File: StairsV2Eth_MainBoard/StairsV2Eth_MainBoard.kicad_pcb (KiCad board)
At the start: 2 copper layers, 102 x 86.2 mm, 104 parts, among them IC1 74HCT08D,653, IC2 74HCT08D,653, J10 Conn_01x02, J11 Conn_01x02, J12 Conn_01x02, J13 Conn_01x02, J14 Conn_01x18, J15 Conn_01x04, J16 Conn_01x04, J2 Conn_01x02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

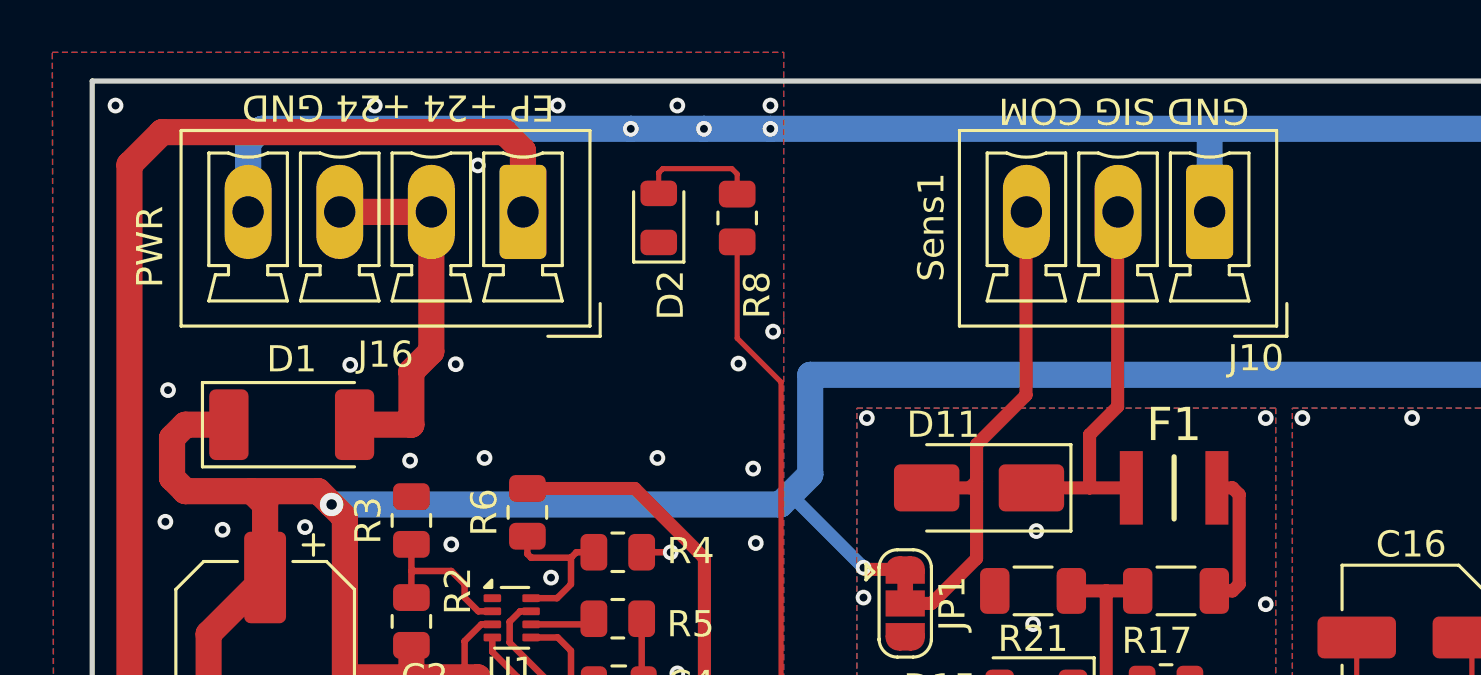
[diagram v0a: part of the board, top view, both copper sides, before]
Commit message: Ethernet on the MCU Board
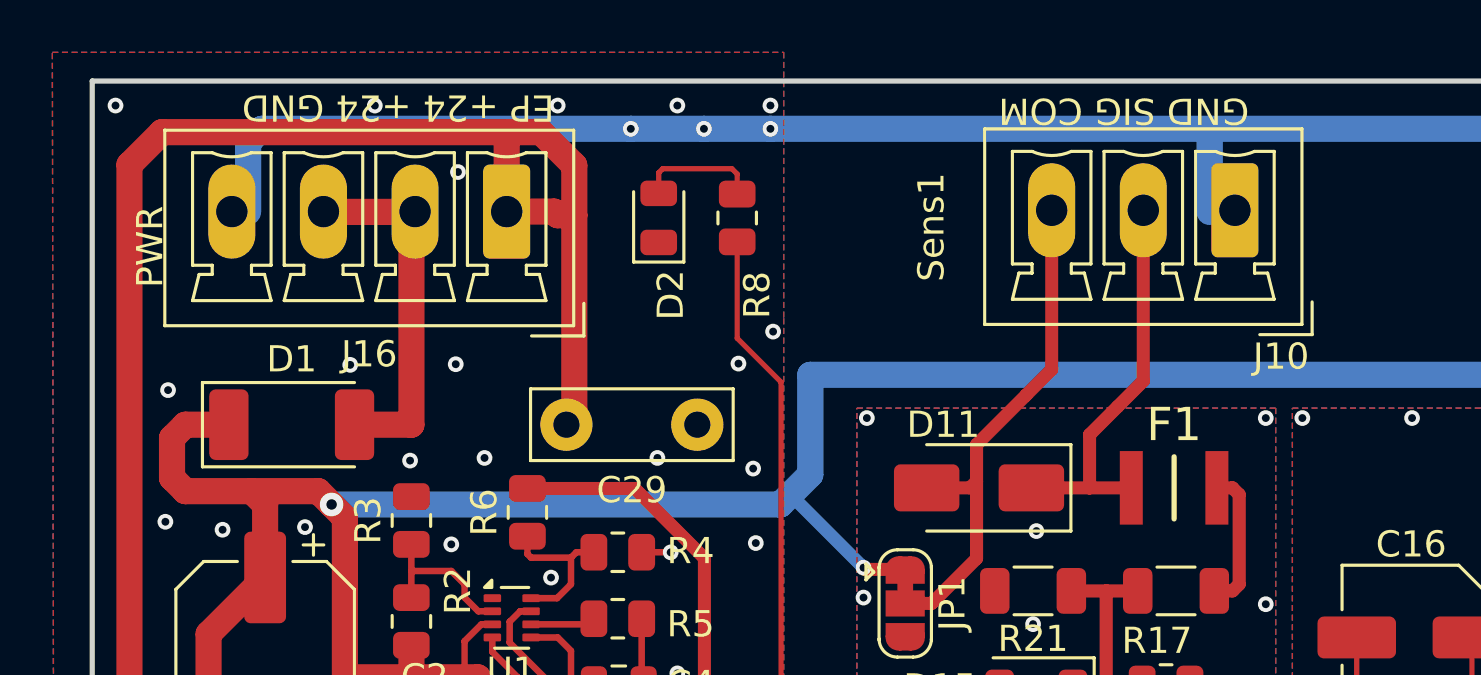
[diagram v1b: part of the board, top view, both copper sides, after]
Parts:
- added C29: 1n 2kV, Capacitor_THT:C_Disc_D7.5mm_W2.5mm_P5.00mm, F.Cu at (137.4, 58.9)
- moved J10 0.97 mm to (158.0, 50.7)
- moved J16 0.62 mm to (130.1, 50.8)
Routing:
- net Earth_Protective: track 73.4 -> 89.5 mm
